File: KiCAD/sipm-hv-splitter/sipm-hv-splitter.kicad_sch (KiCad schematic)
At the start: 4 parts, among them J4 Conn_02x17_Odd_Even, J5 Conn_02x18_Odd_Even, U5 ATmega328-M

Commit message: working on SiPM power supply schem
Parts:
- added C48, C49, C50, C51: 2.2uF, Capacitor_SMD:C_0603_1608Metric_Pad1.08x0.95mm_HandSolder, symbol Device:C
- added U14, U15: MCP1792x-3302xDB, Package_TO_SOT_SMD:SOT-223-3_TabPin2, symbol Regulator_Linear:MCP1792x-3302xDB
- R1: footprint (none) -> Resistor_SMD:R_0603_1608Metric_Pad0.98x0.95mm_HandSolder
- renumbered J5 to J1, J4 to J2, U5 to U1
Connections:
- net +12V: now also C48.1, C50.1, U14.1 (VI), U15.1 (VI)
- net ADC_IMON: now reaches U1.10 (PD6)
- net ADC_VMON: now reaches U1.11 (PD7)
- net ~{SYNC}: now reaches U1.12 (PB0)
- net VR_RESET: now reaches U1.13 (PB1)
- net BOOST_ENA: now reaches U1.14 (PB2)
- net VR_SHDN: now reaches U1.7 (XTAL1/PB6)
- net PGOOD: now reaches U1.8 (XTAL2/PB7)
- net -20V renamed -24V
- new net: C50.2, C51.2, U15.2 (GND)
- new net: C48.2, C49.2, U14.2 (GND)
- new net +3.3V: C49.1, U14.3 (VO)
- new net +3.3VA: C51.1, U15.3 (VO)
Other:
- note added: "3.3V Analog ~40mA max"
- note added: "3.3V Digital ~15mA max"

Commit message: starting placement
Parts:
- removed U14, U15: MCP1792x-3302xDB, Package_TO_SOT_SMD:SOT-223-3_TabPin2, symbol Regulator_Linear:MCP1792x-3302xDB
- added U14, U16: TPS7A25, Package_SON:WSON-6-1EP_2x2mm_P0.65mm_EP1x1.6mm_ThermalVias, symbol my_TPS_LDO:TPS7A25
- C48, C50: value 2.2uF -> 1.0uF
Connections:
- net +12V: now also U14.4 (EN), U14.6 (IN), U16.4 (EN), U16.6 (IN)
- net +3.3V: now also U16.1 (OUT)
- net +3.3VA: now also U14.1 (OUT)
- net at C50.2, C51.2: now also U14.5 (GND), U14.7 (Pad)
- net at C48.2, C49.2: now also U16.5 (GND), U16.7 (Pad)
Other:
- moved on the sheet: C49, C50, C51

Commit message: random placement for area estimate
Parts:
- added C52: 1.0uF, Capacitor_SMD:C_0603_1608Metric_Pad1.08x0.95mm_HandSolder, symbol Device:C
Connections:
- net +3.3V: now also U1.18 (AVCC), U1.4 (VCC), U1.6 (VCC), C52.1
- net GND: now also C48.2, C49.2, C50.2, C51.2, U1.21 (GND), U1.3 (GND), U1.33 (GND), U1.5 (GND), U14.5 (GND), U14.7 (Pad), U16.5 (GND), U16.7 (Pad), C52.2

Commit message: add ISP
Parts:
- added J3: -OMIT-, Connector_PinHeader_1.00mm:PinHeader_1x06_P1.00mm_Vertical, symbol Connector:AVR-ISP-6
- added R45: 4.7k, Resistor_SMD:R_0603_1608Metric_Pad0.98x0.95mm_HandSolder, symbol Device:R_US
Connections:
- net +3.3V: now also J3.2 (VCC), R45.2
- net COMM/RX: now also U1.30 (PD0)
- net COMM/TX: now also U1.31 (PD1)
- net GND: now also J3.6 (GND)
- net MISO: now also J3.1 (MISO)
- net MOSI: now also J3.4 (MOSI)
- net SCK: now also J3.3 (SCK)
- net ~{RESET}: now also J3.5 (~{RST}), R45.1
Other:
- moved on the sheet: C48, C49, C50, C51, C52, U1, U14, U16

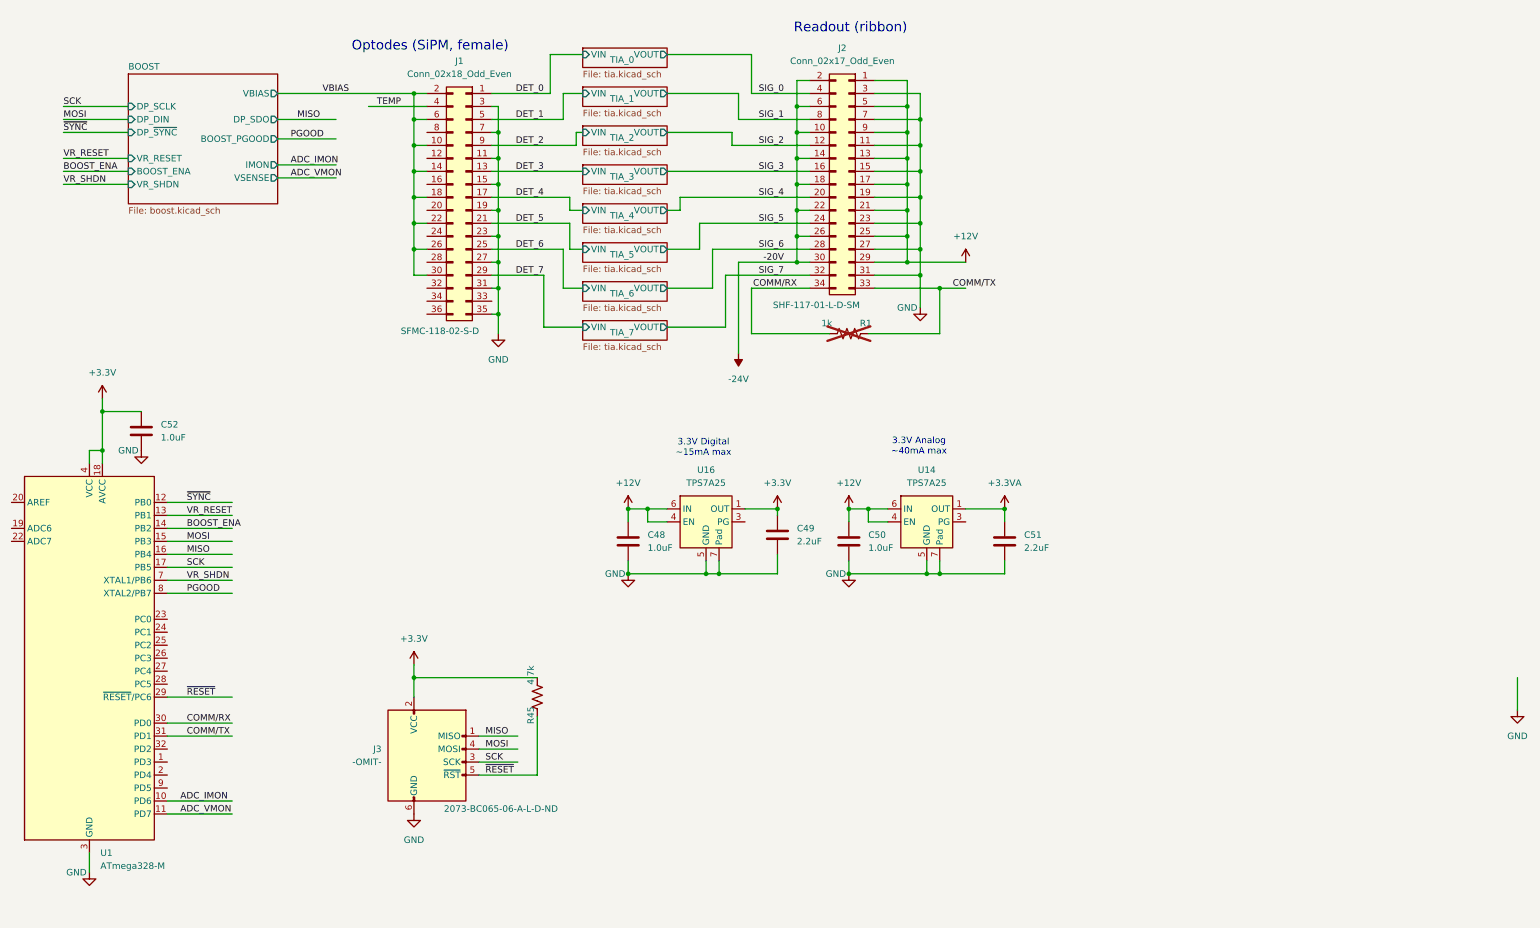
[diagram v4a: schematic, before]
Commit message: fix some MCU pins
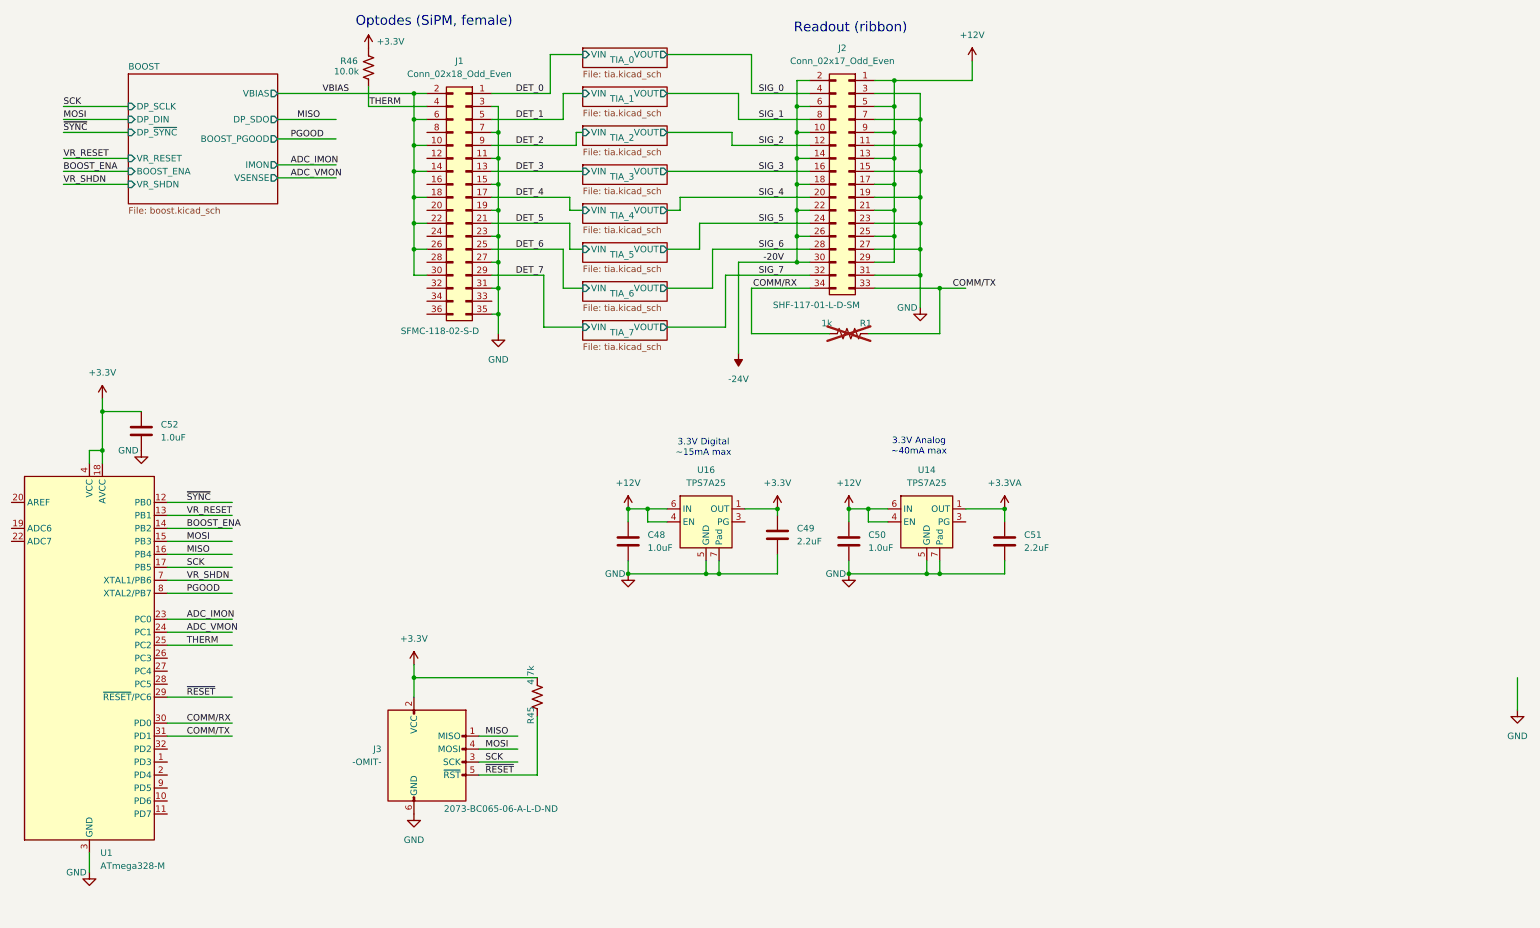
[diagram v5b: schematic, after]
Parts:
- added R46: 10.0k, Resistor_SMD:R_0603_1608Metric_Pad0.98x0.95mm_HandSolder, symbol Device:R_US
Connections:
- net TEMP is gone; now on net THERM: J1.4 (Pin_4)
- net +3.3V: now also R46.2
- net ADC_IMON: now also U1.23 (PC0); no longer U1.10 (PD6)
- net ADC_VMON: now also U1.24 (PC1); no longer U1.11 (PD7)
- net THERM: now reaches U1.25 (PC2)
- net THERM: now also R46.1

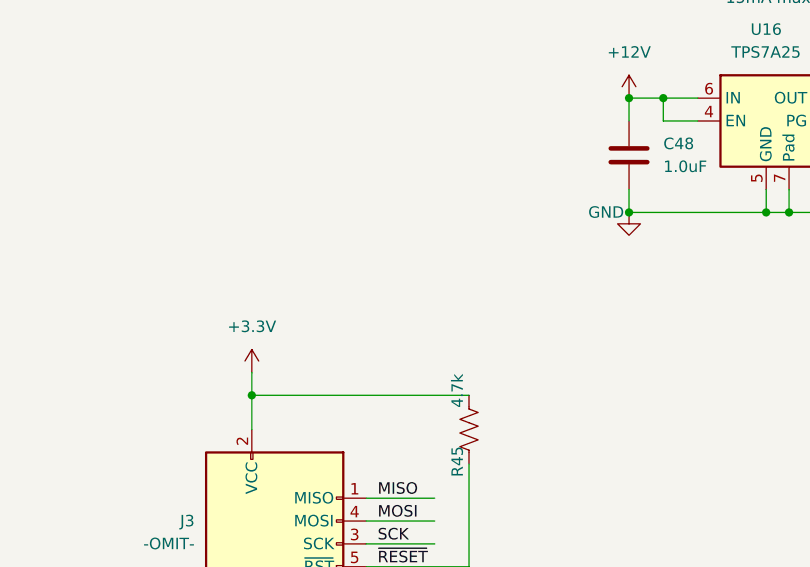
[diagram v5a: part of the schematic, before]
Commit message: working on 2.5 in placement
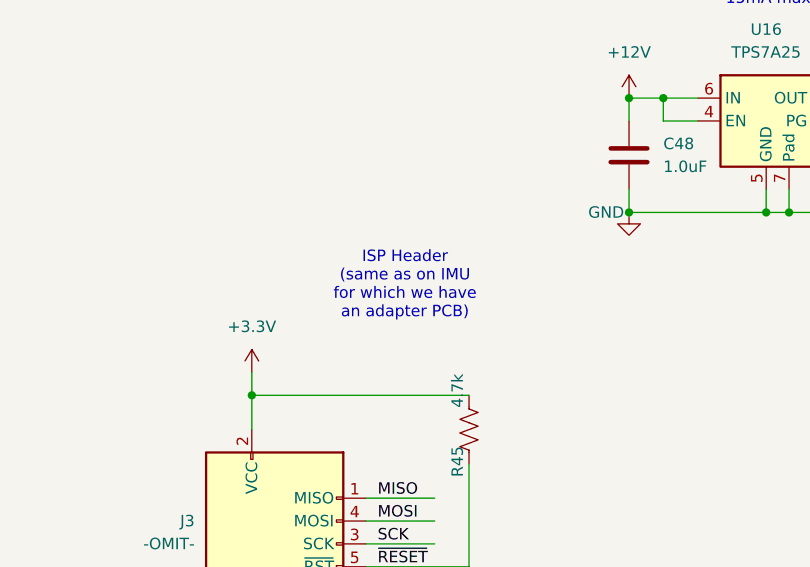
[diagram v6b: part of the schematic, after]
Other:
- note added: "ISP Header (same as on IMU for which we have an adapter PCB)"
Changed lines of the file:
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@@
+		)
+	)
+	(text "ISP Header\n(same as on IMU\nfor which we have\nan adapter PCB)"
+		(exclude_from_sim no)
+		(at 127.508 132.588 0)
+		(effects
+			(font
+				(size 1.27 1.27)
+			)
 		)
 	)

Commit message: routing madness
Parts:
- added D3: LED, my_smt_led:my_SMT_0603, symbol Device:LED
- added R47: 1.5k, Resistor_SMD:R_0603_1608Metric_Pad0.98x0.95mm_HandSolder, symbol Device:R_US
- R1: now fitted
- U1: footprint Package_DFN_QFN:QFN-32-1EP_5x5mm_P0.5mm_EP3.1x3.1mm -> my_QFN:QFN-32-1EP_5x5mm_P0.5mm_EP3.1x3.1mm
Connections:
- net DET_0: now also J1.30 (Pin_30); no longer J1.1 (Pin_1)
- net DET_1: now also J1.26 (Pin_26); no longer J1.5 (Pin_5)
- net DET_2: now also J1.22 (Pin_22); no longer J1.9 (Pin_9)
- net DET_3: now also J1.18 (Pin_18); no longer J1.13 (Pin_13)
- net DET_4: now also J1.14 (Pin_14); no longer J1.17 (Pin_17)
- net DET_5: now also J1.10 (Pin_10); no longer J1.21 (Pin_21)
- net DET_6: now also J1.6 (Pin_6); no longer J1.25 (Pin_25)
- net DET_7: now also J1.2 (Pin_2); no longer J1.29 (Pin_29)
- net GND: now also D3.1 (K); no longer J1.35 (Pin_35)
- net THERM: now also J1.1 (Pin_1); no longer J1.4 (Pin_4)
- net VBIAS: now also J1.12 (Pin_12), J1.16 (Pin_16), J1.20 (Pin_20), J1.24 (Pin_24), J1.28 (Pin_28), J1.32 (Pin_32), J1.4 (Pin_4), J1.8 (Pin_8); no longer J1.10 (Pin_10), J1.14 (Pin_14), J1.18 (Pin_18), J1.2 (Pin_2), J1.22 (Pin_22), J1.26 (Pin_26), J1.30 (Pin_30), J1.6 (Pin_6)
- net at U1.32 (PD2): now also R47.1
- new net: D3.2 (A), R47.2
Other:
- note added: "GP LED"
- moved on the sheet: J1, R46

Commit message: working on bias filter changes
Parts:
- added C53: 1.0uF, Capacitor_SMD:C_0603_1608Metric_Pad1.08x0.95mm_HandSolder, symbol Device:C
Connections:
- net COMM/RX: now also J2.33 (Pin_33), R1.1; no longer J2.34 (Pin_34), R1.2
- net COMM/TX: now also J2.34 (Pin_34), R1.2; no longer J2.33 (Pin_33), R1.1
- net GND: now also C53.2
- net THERM: now also C53.1
- net VBIAS: no longer J1.12 (Pin_12), J1.16 (Pin_16), J1.20 (Pin_20), J1.24 (Pin_24), J1.28 (Pin_28), J1.32 (Pin_32), J1.4 (Pin_4), J1.8 (Pin_8)
- new net TIA_0/SIPM_K: J1.4 (Pin_4)
- new net TIA_1/SIPM_K: J1.8 (Pin_8)
- new net TIA_2/SIPM_K: J1.12 (Pin_12)
- new net TIA_3/SIPM_K: J1.16 (Pin_16)
- new net TIA_4/SIPM_K: J1.20 (Pin_20)
- new net TIA_5/SIPM_K: J1.24 (Pin_24)
- new net TIA_7/SIPM_K: J1.32 (Pin_32)
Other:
- sheet TIA_0 ports: added SIPM_A, SIPM_K, VBIAS; removed VIN
- sheet TIA_1 ports: added SIPM_A, SIPM_K, VBIAS; removed VIN
- sheet TIA_2 ports: added SIPM_A, SIPM_K, VBIAS; removed VIN
- sheet TIA_3 ports: added SIPM_A, SIPM_K, VBIAS; removed VIN
- sheet TIA_4 ports: added SIPM_A, SIPM_K, VBIAS; removed VIN
- sheet TIA_5 ports: added SIPM_A, SIPM_K, VBIAS; removed VIN
- sheet TIA_6 ports: added SIPM_A, SIPM_K, VBIAS; removed VIN
- sheet TIA_7 ports: added SIPM_A, SIPM_K, VBIAS; removed VIN
- note added: "ISP Header (1mm) (same as on IMU for which we have an adapter PCB)"
- note added: "Readout (ribbon, male)"
- note removed: "ISP Header (same as on IMU for which we have an adapter PCB)"
- note removed: "Readout (ribbon)"
- moved on the sheet: C48, C49, C50, C51, J2, J3, R1, R45, U14, U16
